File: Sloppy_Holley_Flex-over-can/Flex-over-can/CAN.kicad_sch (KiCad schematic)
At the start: 7 parts, among them U8 TJA1051T/3

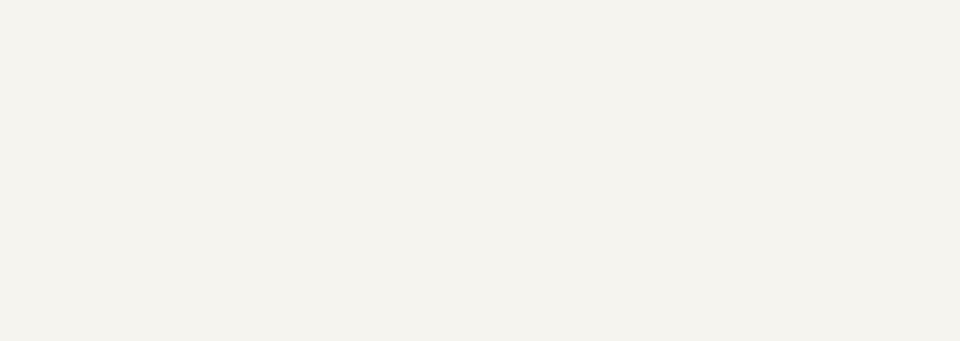
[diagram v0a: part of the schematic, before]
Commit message: Add PCB placement notes for decoupling caps to each sheet
Co-Authored-By: Claude Opus 5.5 <noreply@anthropic.com>
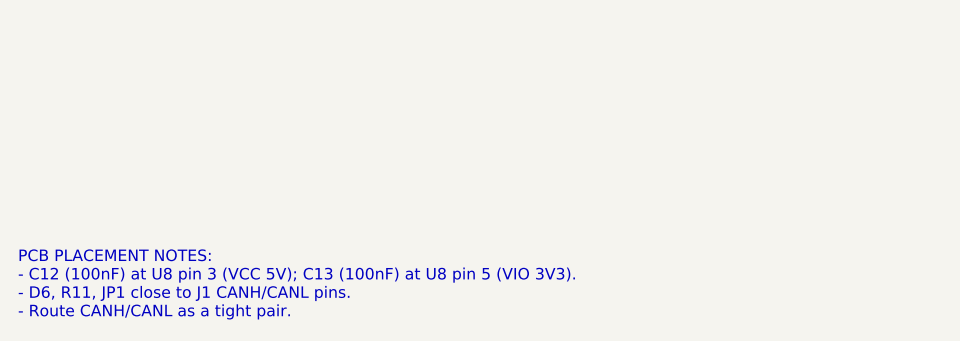
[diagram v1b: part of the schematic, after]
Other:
- note added: "PCB PLACEMENT NOTES: - C12 (100nF) at U8 pin 3 (VCC 5V); C13 (100nF) at U8 pin 5 (VIO 3V3). - D6, R11, JP1 close to J1 CANH/CANL pins. - Route CANH/CANL as a tight pair."
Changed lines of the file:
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@@
 		)
 	)
+  (text "PCB PLACEMENT NOTES:\n- C12 (100nF) at U8 pin 3 (VCC 5V); C13 (100nF) at U8 pin 5 (VIO 3V3).\n- D6, R11, JP1 close to J1 CANH/CANL pins.\n- Route CANH/CANL as a tight pair."
+    (at 15.24 180.34 0)
+    (effects (font (size 1.27 1.27) (color 0 0 194 1)) (justify left bottom))
+  )
 	(symbol
 		(lib_id "Device:C")
